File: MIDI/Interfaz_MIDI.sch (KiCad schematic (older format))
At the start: 22 parts, among them J1 DIN_5, J2 DIN_5, J3 DIN_5, U1 6N138, U2 4050

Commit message: Se continuan las correciones correspondientes a la 1ra revisión
> Se realizan los cambios necesarios para la utilización de la biblioteca de huellas autocontenidas.
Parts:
- C1, C2, C3: footprint Capacitors_SMD:C_0603_HandSoldering -> MIDI:C_0805_HandSoldering
- D1: footprint Diodes_THT:D_DO-35_SOD27_P7.62mm_Horizontal -> MIDI:D_DO-35_SOD27_P7.62mm_Horizontal
- FB1, FB2, FB3, FB4, FB5, FB6: footprint Resistors_SMD:R_0805_HandSoldering -> MIDI:FB_0805_HandSoldering
- R1, R4, R5, R7: footprint Resistors_SMD:R_0603_HandSoldering -> MIDI:R_0805_HandSoldering
- R2, R3, R6: footprint Resistors_SMD:R_0805_HandSoldering -> MIDI:R_0805_HandSoldering
- U1: footprint Housings_DIP:DIP-8_W7.62mm -> MIDI:DIP-8_W7.62mm_LongPads
- U2: footprint Housings_DIP:DIP-16_W7.62mm_LongPads -> MIDI:DIP-16_W7.62mm_LongPads
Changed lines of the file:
@@
 F 0 "FB3" H 3465 3185 60  0000 C CNN
 F 1 "1k @100MHz" H 3465 2935 60  0000 C CNN
-F 2 "Resistors_SMD:R_0805_HandSoldering" H 3465 3035 60  0001 C CNN
+F 2 "MIDI:FB_0805_HandSoldering" H 3465 3035 60  0001 C CNN
 F 3 "http://ds.yuden.co.jp/TYCOMPAS/ut/detail.do?productNo=BK2125HS102-T&fileName=BK2125HS102-T_SS&mode=specSheetDownload" H 3465 3035 60  0001 C CNN
 F 4 "FERRITE BEAD 1 KOHM 0805 1LN" H 0   0   50  0001 C CNN "Desc"
@@
 F 0 "FB1" H 3465 2375 60  0000 C CNN
 F 1 "1k @100MHz" H 3465 2125 60  0000 C CNN
-F 2 "Resistors_SMD:R_0805_HandSoldering" H 3465 2225 60  0001 C CNN
+F 2 "MIDI:FB_0805_HandSoldering" H 3465 2225 60  0001 C CNN
 F 3 "http://ds.yuden.co.jp/TYCOMPAS/ut/detail.do?productNo=BK2125HS102-T&fileName=BK2125HS102-T_SS&mode=specSheetDownload" H 3465 2225 60  0001 C CNN
 F 4 "FERRITE BEAD 1 KOHM 0805 1LN" H 0   0   50  0001 C CNN "Desc"
@@
 F 0 "FB2" H 8345 2850 60  0000 C CNN
 F 1 "1k @100MHz" H 8345 2600 60  0000 C CNN
-F 2 "Resistors_SMD:R_0805_HandSoldering" H 8345 2700 60  0001 C CNN
+F 2 "MIDI:FB_0805_HandSoldering" H 8345 2700 60  0001 C CNN
 F 3 "http://ds.yuden.co.jp/TYCOMPAS/ut/detail.do?productNo=BK2125HS102-T&fileName=BK2125HS102-T_SS&mode=specSheetDownload" H 8345 2700 60  0001 C CNN
 F 4 "FERRITE BEAD 1 KOHM 0805 1LN" H 0   0   50  0001 C CNN "Desc"
@@
 F 0 "FB4" H 8345 3650 60  0000 C CNN
 F 1 "1k @100MHz" H 8345 3400 60  0000 C CNN
-F 2 "Resistors_SMD:R_0805_HandSoldering" H 8345 3500 60  0001 C CNN
+F 2 "MIDI:FB_0805_HandSoldering" H 8345 3500 60  0001 C CNN
 F 3 "http://ds.yuden.co.jp/TYCOMPAS/ut/detail.do?productNo=BK2125HS102-T&fileName=BK2125HS102-T_SS&mode=specSheetDownload" H 8345 3500 60  0001 C CNN
 F 4 "FERRITE BEAD 1 KOHM 0805 1LN" H 0   0   50  0001 C CNN "Desc"
@@
 F 0 "R2" V 7815 2280 40  0000 C CNN
 F 1 "33R 0,5W" V 7742 2281 40  0000 C CNN
-F 2 "Resistors_SMD:R_0805_HandSoldering" V 7665 2280 30  0001 C CNN
+F 2 "MIDI:R_0805_HandSoldering" V 7665 2280 30  0001 C CNN
 F 3 "https://industrial.panasonic.com/cdbs/www-data/pdf/RDO0000/AOA0000C291.pdf" H 7735 2280 30  0001 C CNN
 F 4 "RES SMD 33 OHM 5% 1/2W 0805" H 0   0   50  0001 C CNN "Desc"
@@
 F 0 "R5" V 7575 3500 40  0000 C CNN
 F 1 "10R" V 7502 3501 40  0000 C CNN
-F 2 "Resistors_SMD:R_0603_HandSoldering" V 7425 3500 30  0001 C CNN
+F 2 "MIDI:R_0805_HandSoldering" V 7425 3500 30  0001 C CNN
 F 3 "http://www.rohm.com/web/global/datasheet/ESR01MZPF/esr-e" H 7495 3500 30  0001 C CNN
 F 4 "RES SMD 10 OHM 5% 1/4W 0603" H 0   0   50  0001 C CNN "Desc"
@@
 F 0 "FB6" H 8345 5875 60  0000 C CNN
 F 1 "1k @100MHz" H 8345 5625 60  0000 C CNN
-F 2 "Resistors_SMD:R_0805_HandSoldering" H 8345 5725 60  0001 C CNN
+F 2 "MIDI:FB_0805_HandSoldering" H 8345 5725 60  0001 C CNN
 F 3 "http://ds.yuden.co.jp/TYCOMPAS/ut/detail.do?productNo=BK2125HS102-T&fileName=BK2125HS102-T_SS&mode=specSheetDownload" H 8345 5725 60  0001 C CNN
 F 4 "FERRITE BEAD 1 KOHM 0805 1LN" H 0   0   50  0001 C CNN "Desc"
@@
 F 0 "R6" V 7815 4505 40  0000 C CNN
 F 1 "33R 0,5W" V 7742 4506 40  0000 C CNN
-F 2 "Resistors_SMD:R_0805_HandSoldering" V 7665 4505 30  0001 C CNN
+F 2 "MIDI:R_0805_HandSoldering" V 7665 4505 30  0001 C CNN
 F 3 "https://industrial.panasonic.com/cdbs/www-data/pdf/RDO0000/AOA0000C291.pdf" H 7735 4505 30  0001 C CNN
 F 4 "RES SMD 33 OHM 5% 1/2W 0805" H 0   0   50  0001 C CNN "Desc"
@@
 F 0 "R7" V 7575 5725 40  0000 C CNN
 F 1 "10R" V 7502 5726 40  0000 C CNN
-F 2 "Resistors_SMD:R_0603_HandSoldering" V 7425 5725 30  0001 C CNN
+F 2 "MIDI:R_0805_HandSoldering" V 7425 5725 30  0001 C CNN
 F 3 "http://www.rohm.com/web/global/datasheet/ESR01MZPF/esr-e" H 7495 5725 30  0001 C CNN
 F 4 "RES SMD 10 OHM 5% 1/4W 0603" H 0   0   50  0001 C CNN "Desc"
@@
 F 0 "FB5" H 8345 5075 60  0000 C CNN
 F 1 "1k @100MHz" H 8345 4825 60  0000 C CNN
-F 2 "Resistors_SMD:R_0805_HandSoldering" H 8345 4925 60  0001 C CNN
+F 2 "MIDI:FB_0805_HandSoldering" H 8345 4925 60  0001 C CNN
 F 3 "http://ds.yuden.co.jp/TYCOMPAS/ut/detail.do?productNo=BK2125HS102-T&fileName=BK2125HS102-T_SS&mode=specSheetDownload" H 8345 4925 60  0001 C CNN
 F 4 "FERRITE BEAD 1 KOHM 0805 1LN" H 0   0   50  0001 C CNN "Desc"
@@
 F 0 "U1" H 4655 2950 50  0000 L CNN
 F 1 "6N138" H 4730 2300 50  0000 L CNN
-F 2 "Housings_DIP:DIP-8_W7.62mm" H 4655 2250 50  0001 L CIN
+F 2 "MIDI:DIP-8_W7.62mm_LongPads" H 4655 2250 50  0001 L CIN
 F 3 "/Datasheets/6n138.pdf" V 4880 2600 50  0001 L CNN
 F 4 "OPTOISO 5KV DARL W/BASE 8DIP" H 0   0   50  0001 C CNN "Desc"
@@
 F 0 "D1" H 4065 2735 40  0000 C CNN
 F 1 "1N4148" H 4065 2535 40  0000 C CNN
-F 2 "Diodes_THT:D_DO-35_SOD27_P7.62mm_Horizontal" H 4065 2635 60  0001 C CNN
+F 2 "MIDI:D_DO-35_SOD27_P7.62mm_Horizontal" H 4065 2635 60  0001 C CNN
 F 3 "https://www.fairchildsemi.com/datasheets/1N/1N914.pdf" H 4065 2635 60  0001 C CNN
 F 4 "DIODE GEN PURP 100V 200MA DO35" H 0   0   50  0001 C CNN "Desc"
@@
 F 0 "C2" H 2310 3445 40  0000 L CNN
 F 1 "100nF" H 2316 3260 40  0000 L CNN
-F 2 "Capacitors_SMD:C_0603_HandSoldering" H 2348 3195 30  0001 C CNN
+F 2 "MIDI:C_0805_HandSoldering" H 2348 3195 30  0001 C CNN
 F 3 "http://search.murata.co.jp/Ceramy/image/img/A01X/G101/ENG/GRM188R71C104KA01-01.pdf" H 2310 3345 60  0001 C CNN
 F 4 "CAP CER 0.1UF 16V X7R 0603 " H 0   0   50  0001 C CNN "Desc"
@@
 F 0 "C1" H 1310 3445 40  0000 L CNN
 F 1 "100nF" H 1316 3260 40  0000 L CNN
-F 2 "Capacitors_SMD:C_0603_HandSoldering" H 1348 3195 30  0001 C CNN
+F 2 "MIDI:C_0805_HandSoldering" H 1348 3195 30  0001 C CNN
 F 3 "http://search.murata.co.jp/Ceramy/image/img/A01X/G101/ENG/GRM188R71C104KA01-01.pdf" H 1310 3345 60  0001 C CNN
 F 4 "CAP CER 0.1UF 16V X7R 0603 " H 0   0   50  0001 C CNN "Desc"
@@
 F 0 "R1" V 5675 2145 40  0000 C CNN
 F 1 "1K" V 5602 2146 40  0000 C CNN
-F 2 "Resistors_SMD:R_0603_HandSoldering" V 5525 2145 30  0001 C CNN
+F 2 "MIDI:R_0805_HandSoldering" V 5525 2145 30  0001 C CNN
 F 3 "http://www.rohm.com/web/global/datasheet/ESR01MZPF/esr-e" H 5595 2145 30  0001 C CNN
 F 4 "RES SMD 1K OHM 5% 1/4W 0603 " H 0   0   50  0001 C CNN "Desc"
@@
 F 0 "R4" V 5465 3285 40  0000 C CNN
 F 1 "4K7" V 5392 3286 40  0000 C CNN
-F 2 "Resistors_SMD:R_0603_HandSoldering" V 5315 3285 30  0001 C CNN
+F 2 "MIDI:R_0805_HandSoldering" V 5315 3285 30  0001 C CNN
 F 3 "http://www.rohm.com/web/global/datasheet/ESR01MZPF/esr-e" H 5385 3285 30  0001 C CNN
 F 4 "RES SMD 4.7K OHM 5% 1/4W 0603 " H 0   0   50  0001 C CNN "Desc"
@@
 F 0 "U2" H 2045 5165 50  0000 C CNN
 F 1 "4050" H 2040 4925 50  0000 C CNN
-F 2 "Housings_DIP:DIP-16_W7.62mm_LongPads" H 1850 5050 60  0001 C CNN
+F 2 "MIDI:DIP-16_W7.62mm_LongPads" H 1850 5050 60  0001 C CNN
 F 3 "/Datasheets/cd4050b.pdf" H 1850 5050 60  0001 C CNN
 F 4 "IC BUFF/CONVERTER HEX 16DIP" H -4695 1550 50  0001 C CNN "Desc"
@@
 F 0 "U2" H 6740 2815 50  0000 C CNN
 F 1 "4050" H 6735 2575 50  0000 C CNN
-F 2 "Housings_DIP:DIP-16_W7.62mm_LongPads" H 6545 2700 60  0001 C CNN
+F 2 "MIDI:DIP-16_W7.62mm_LongPads" H 6545 2700 60  0001 C CNN
 F 3 "/Datasheets/cd4050b.pdf" H 6545 2700 60  0001 C CNN
 F 4 "IC BUFF/CONVERTER HEX 16DIP" H 0   0   50  0001 C CNN "Desc"
@@
 F 0 "U2" H 6740 3615 50  0000 C CNN
 F 1 "4050" H 6735 3375 50  0000 C CNN
-F 2 "Housings_DIP:DIP-16_W7.62mm_LongPads" H 6545 3500 60  0001 C CNN
+F 2 "MIDI:DIP-16_W7.62mm_LongPads" H 6545 3500 60  0001 C CNN
 F 3 "/Datasheets/cd4050b.pdf" H 6545 3500 60  0001 C CNN
 F 4 "IC BUFF/CONVERTER HEX 16DIP" H 0   -2225 50  0001 C CNN "Desc"
@@
 F 0 "R3" V 2865 3035 40  0000 C CNN
 F 1 "220R" V 2792 3036 40  0000 C CNN
-F 2 "Resistors_SMD:R_0805_HandSoldering" V 2715 3035 30  0001 C CNN
+F 2 "MIDI:R_0805_HandSoldering" V 2715 3035 30  0001 C CNN
 F 3 "http://www.rohm.com/web/global/datasheet/ESR01MZPF/esr-e" H 2785 3035 30  0001 C CNN
 F 4 "RES SMD 220 OHM 5% 1/4W 0603" H 0   0   50  0001 C CNN "Desc"
@@
 F 0 "C3" H 3660 5030 40  0000 L CNN
 F 1 "100nF" H 3666 4845 40  0000 L CNN
-F 2 "Capacitors_SMD:C_0603_HandSoldering" H 3698 4780 30  0001 C CNN
+F 2 "MIDI:C_0805_HandSoldering" H 3698 4780 30  0001 C CNN
 F 3 "http://search.murata.co.jp/Ceramy/image/img/A01X/G101/ENG/GRM188R71C104KA01-01.pdf" H 3660 4930 60  0001 C CNN
 F 4 "CAP CER 0.1UF 16V X7R 0603 " H -2900 -2150 50  0001 C CNN "Desc"
@@
 F 0 "U2" H 2045 4765 50  0000 C CNN
 F 1 "4050" H 2040 4525 50  0000 C CNN
-F 2 "Housings_DIP:DIP-16_W7.62mm_LongPads" H 1850 4650 60  0001 C CNN
+F 2 "MIDI:DIP-16_W7.62mm_LongPads" H 1850 4650 60  0001 C CNN
 F 3 "/Datasheets/cd4050b.pdf" H 1850 4650 60  0001 C CNN
 F 4 "IC BUFF/CONVERTER HEX 16DIP" H 0   0   50  0001 C CNN "Desc"
@@
 F 0 "U2" H 6740 5840 50  0000 C CNN
 F 1 "4050" H 6735 5600 50  0000 C CNN
-F 2 "Housings_DIP:DIP-16_W7.62mm_LongPads" H 6545 5725 60  0001 C CNN
+F 2 "MIDI:DIP-16_W7.62mm_LongPads" H 6545 5725 60  0001 C CNN
 F 3 "/Datasheets/cd4050b.pdf" H 6545 5725 60  0001 C CNN
 F 4 "IC BUFF/CONVERTER HEX 16DIP" H 4695 675 50  0001 C CNN "Desc"
@@
 F 0 "U2" H 2045 5565 50  0000 C CNN
 F 1 "4050" H 2040 5325 50  0000 C CNN
-F 2 "Housings_DIP:DIP-16_W7.62mm_LongPads" H 1850 5450 60  0001 C CNN
+F 2 "MIDI:DIP-16_W7.62mm_LongPads" H 1850 5450 60  0001 C CNN
 F 3 "/Datasheets/cd4050b.pdf" H 1850 5450 60  0001 C CNN
 F 4 "IC BUFF/CONVERTER HEX 16DIP" H 0   0   50  0001 C CNN "Desc"

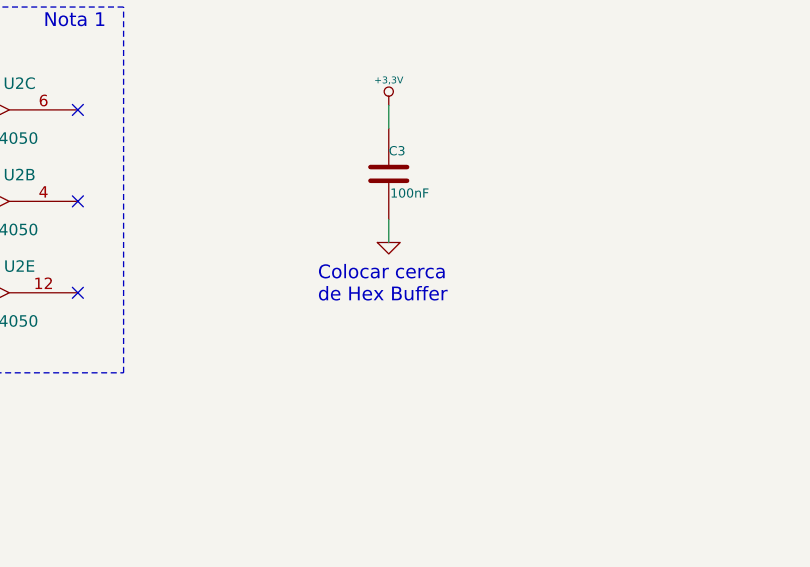
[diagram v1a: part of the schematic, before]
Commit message: Se avanza con primera iteración de ruteo
> Se terminan de rutear conexiones para estudiar factibilidad de placement.
> Para facilitar el ruteo se realizan los siguientes cambios:
  > Se desconecta pin redundante de tact-switch's para permitir la conexión entre planos de masa.
  > Se desconectan pines del conector derecho de forma que no requieran ser ruteados a los homologos del conector izquierdo.
  > Se intercambian unidades F y D del componente 40106.
  > Se agrupan señales de los interruptores de los encoders en vez de intercalarlos con las señales de encoder, propiamente dicho, de cada uno. Se rutean a pines superiores en el conector izquierdo, mientras se desplazan las restantes señales hacia abajo.

> Se aguarda comentarios de los revisores para emprolijar, embellecer y mejorar el ruteo.
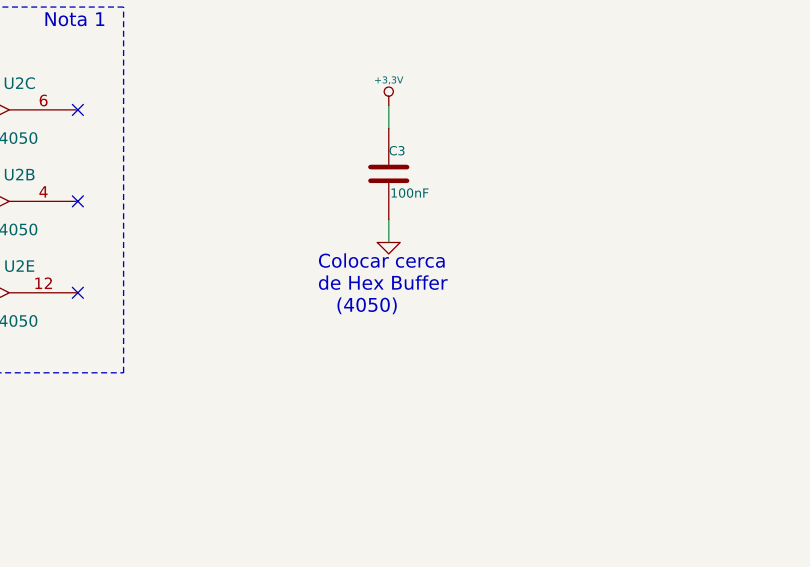
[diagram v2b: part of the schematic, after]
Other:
- note added: "Colocar cerca\nde Hex Buffer\n (4050)"
- note removed: "Colocar cerca\nde Hex Buffer"
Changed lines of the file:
@@
 Text Notes 9620 2230 0    60   ~ 0
 MIDI THRU
-Text Notes 3350 5500 0    60   ~ 0
-Colocar cerca\nde Hex Buffer
+Text Notes 3350 5550 0    60   ~ 0
+Colocar cerca\nde Hex Buffer\n   (4050)
 Text Notes 2150 4300 0    60   ~ 0
 Nota 1

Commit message: Se modifican campos de componentes
> Se realizan los cambios en los campos de kiCost para reflejar los cambios de footprints (de 0603 a 0805).
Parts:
- C1, C2, C3: Desc CAP CER 0.1UF 16V X7R 0603 -> CAP CER 0.1UF 50V X7R 0805; Digikey# 490-1532-1-ND -> 311-1140-1-ND; Manf Murata Electronics North America -> Yageo; Manf# GRM188R71C104KA01D -> CC0805KRX7R9BB104; Mouser# 81-GRM39X104K16 -> 603-CC805KRX7R9BB104
- R1: Desc RES SMD 1K OHM 5% 1/4W 0603 -> RES SMD 1K OHM 1% 1/2W 0805; Digikey# RHM1.0KDCT-ND -> P16885CT-ND; Manf Rohm Semiconductor -> Panasonic Electronic Components; Manf# ESR03EZPJ102 -> ERJ-P6WF1001V; Mouser# 755-ESR03EZPJ102 -> 667-ERJ-P6WF1001V
- R3: Desc RES SMD 220 OHM 5% 1/4W 0603 -> RES SMD 220 OHM 5% 1/2W 0805; Digikey# RHM220DCT-ND -> P220ADCT-ND; Manf Rohm Semiconductor -> Panasonic Electronic Components; Manf# ESR03EZPJ221 -> ERJ-P06J221V; Mouser# 755-ESR03EZPJ221 -> 667-ERJ-P06J221V
- R4: Desc RES SMD 4.7K OHM 5% 1/4W 0603 -> RES SMD 4.7K OHM 5% 1/2W 0805; Digikey# RHM4.7KDCT-ND -> P4.7KADCT-ND; Manf Rohm Semiconductor -> Panasonic Electronic Components; Manf# ESR03EZPJ472 -> ERJ-P06J472V; Mouser# 755-ESR03EZPJ472 -> 667-ERJ-P06J472V
- R5, R7: Desc RES SMD 10 OHM 5% 1/4W 0603 -> RES SMD 1K OHM 1% 1/4W 0805; Digikey# RHM10DCT-ND -> CRS0805-FX-1001ELFCT-ND; Manf Rohm Semiconductor -> Bourns Inc.; Manf# ESR03EZPJ100 -> CRS0805-FX-1001ELF; Mouser# 755-ESR03EZPJ100 -> 652-CRS0805FX1001ELF

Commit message: Correcciones menores en campos para BOM
> Se corrigen error observados luego de la generación de la BOM.
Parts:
- C1, C2, C3: Description (none) -> CAP CER 0.1UF 50V X7R 0805
- D1: Description (none) -> DIODE GEN PURP 100V 200MA DO35; Manf# 1N4148 -> 1N4148
- FB1, FB2, FB3, FB4, FB5, FB6: Description (none) -> FERRITE BEAD 1 KOHM 0805 1LN
- J1, J2, J3: Desc CONN DIN 5POS FEMALE SHIELDED -> CONN DIN 5POS FEMALE SHIELDED; Description (none) -> CONN DIN 5POS FEMALE SHIELDED; Digikey# CP-7050-ND -> CP-7050-ND
- R1: Description (none) -> RES SMD 1K OHM 1% 1/2W 0805
- R2, R6: Description (none) -> RES SMD 33 OHM 5% 1/2W 0805
- R3: Description (none) -> RES SMD 220 OHM 5% 1/2W 0805
- R4: Description (none) -> RES SMD 4.7K OHM 5% 1/2W 0805
- R5, R7: Description (none) -> RES SMD 1K OHM 1% 1/4W 0805
- U1: Description (none) -> OPTOISO 5KV DARL W/BASE 8DIP
- U2: Description (none) -> IC BUFF/CONVERTER HEX 16DIP

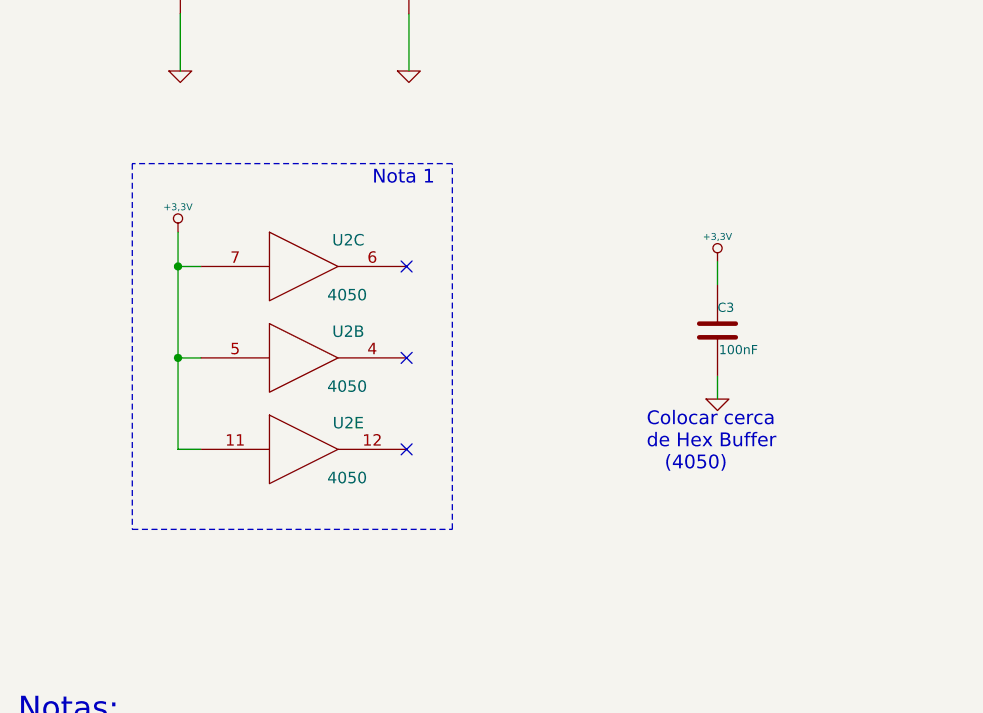
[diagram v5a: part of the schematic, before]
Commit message: Se finalizan los cambios según las revisiones
> Se realizan cambios segun detalles en archivos de revisiones.
> Se abandona requisito para asegurar fabricación artesanal por lo que se comienzan a utilizar los orificios metalizados para rutear.
> Se cambia la tensión de fijación de las compuertas no utilizadas en el 4050 para mejorar el plano de masa debajo del mismo.
> Se genera la versión 1.0 del diseño.
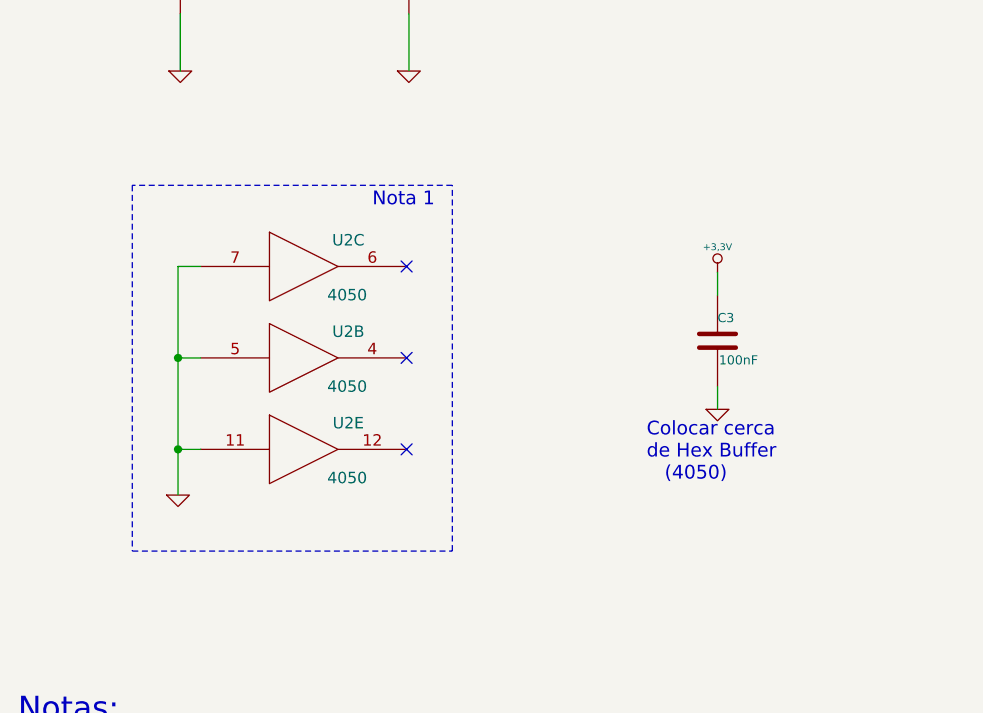
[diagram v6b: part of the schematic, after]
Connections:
- net +3.3V: no longer U2.11, U2.5, U2.7
- net GND: now also U2.11, U2.5, U2.7
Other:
- moved on the sheet: C3
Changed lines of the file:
@@
 L GND #PWR014
 U 1 1 592CE7E7
-P 3660 5230
-F 0 "#PWR014" H 3660 5230 30  0001 C CNN
-F 1 "GND" H 3660 5160 30  0001 C CNN
-F 2 "" H 3660 5230 60  0000 C CNN
-F 3 "" H 3660 5230 60  0000 C CNN
-	1    3660 5230
+P 3660 5275
+F 0 "#PWR014" H 3660 5275 30  0001 C CNN
+F 1 "GND" H 3660 5205 30  0001 C CNN
+F 2 "" H 3660 5275 60  0000 C CNN
+F 3 "" H 3660 5275 60  0000 C CNN
+	1    3660 5275
 	1    0    0    -1
 $EndComp
@@
 L +3,3V #PWR015
 U 1 1 592CE837
-P 3660 4630
-F 0 "#PWR015" H 3660 4590 30  0001 C CNN
-F 1 "+3,3V" H 3660 4740 30  0000 C CNN
-F 2 "" H 3660 4630 60  0000 C CNN
-F 3 "" H 3660 4630 60  0000 C CNN
-	1    3660 4630
+P 3660 4675
+F 0 "#PWR015" H 3660 4635 30  0001 C CNN
+F 1 "+3,3V" H 3660 4785 30  0000 C CNN
+F 2 "" H 3660 4675 60  0000 C CNN
+F 3 "" H 3660 4675 60  0000 C CNN
+	1    3660 4675
 	1    0    0    -1
 $EndComp
@@
 L C C3
 U 1 1 592CE8FA
-P 3660 4930
-F 0 "C3" H 3660 5030 40  0000 L CNN
-F 1 "100nF" H 3666 4845 40  0000 L CNN
-F 2 "MIDI:C_0805_HandSoldering" H 3698 4780 30  0001 C CNN
-F 3 "http://www.yageo.com/documents/recent/UPY-GPHC_X7R_6.3V-to-50V_18.pdf" H 3660 4930 60  0001 C CNN
-F 4 "CAP CER 0.1UF 50V X7R 0805" H 0   0   50  0001 C CNN "Desc"
-F 5 "CAP CER 0.1UF 50V X7R 0805" H 0   0   50  0001 C CNN "Description"
-F 6 "311-1140-1-ND" H -2900 -2150 50  0001 C CNN "Digikey#"
-F 7 "Yageo" H -2900 -2150 50  0001 C CNN "Manf"
-F 8 "CC0805KRX7R9BB104" H -2900 -2150 50  0001 C CNN "Manf#"
-F 9 "603-CC805KRX7R9BB104" H -2900 -2150 50  0001 C CNN "Mouser#"
-	1    3660 4930
-	1    0    0    -1
-$EndComp
-$Comp
-L +3,3V #PWR016
-U 1 1 592EB13E
-P 1300 4500
-F 0 "#PWR016" H 1300 4460 30  0001 C CNN
-F 1 "+3,3V" H 1300 4610 30  0000 C CNN
-F 2 "" H 1300 4500 60  0000 C CNN
-F 3 "" H 1300 4500 60  0000 C CNN
-	1    1300 4500
+P 3660 4975
+F 0 "C3" H 3660 5075 40  0000 L CNN
+F 1 "100nF" H 3666 4890 40  0000 L CNN
+F 2 "MIDI:C_0805_HandSoldering" H 3698 4825 30  0001 C CNN
+F 3 "http://www.yageo.com/documents/recent/UPY-GPHC_X7R_6.3V-to-50V_18.pdf" H 3660 4975 60  0001 C CNN
+F 4 "CAP CER 0.1UF 50V X7R 0805" H 0   45  50  0001 C CNN "Desc"
+F 5 "CAP CER 0.1UF 50V X7R 0805" H 0   45  50  0001 C CNN "Description"
+F 6 "311-1140-1-ND" H -2900 -2105 50  0001 C CNN "Digikey#"
+F 7 "Yageo" H -2900 -2105 50  0001 C CNN "Manf"
+F 8 "CC0805KRX7R9BB104" H -2900 -2105 50  0001 C CNN "Manf#"
+F 9 "603-CC805KRX7R9BB104" H -2900 -2105 50  0001 C CNN "Mouser#"
+	1    3660 4975
 	1    0    0    -1
 $EndComp
@@
 Text Notes 9620 2230 0    60   ~ 0
 MIDI THRU
-Text Notes 3350 5550 0    60   ~ 0
+Text Notes 3350 5595 0    60   ~ 0
 Colocar cerca\nde Hex Buffer\n   (4050)
-Text Notes 2150 4300 0    60   ~ 0
+Text Notes 2150 4395 0    60   ~ 0
 Nota 1
 Text Notes 600  6650 0    100  ~ 0
@@
 	6495 5825 6495 5925
 Wire Wire Line
-	3660 5130 3660 5230
-Wire Wire Line
-	3660 4730 3660 4630
-Wire Wire Line
-	1300 4500 1300 5450
+	3660 5175 3660 5275
+Wire Wire Line
+	3660 4775 3660 4675
 Wire Wire Line
 	1300 5450 1400 5450
@@
 	1400 5050 1300 5050
 Wire Notes Line
-	1100 4200 1100 5800
-Wire Notes Line
-	1100 5800 2500 5800
-Wire Notes Line
-	2500 5800 2500 4200
-Wire Notes Line
-	2500 4200 1100 4200
+	1100 4295 1100 5895
+Wire Notes Line
+	1100 5895 2500 5895
+Wire Notes Line
+	2500 5895 2500 4295
+Wire Notes Line
+	2500 4295 1100 4295
 Connection ~ 4065 3035
 Connection ~ 4065 2225
 Connection ~ 5595 2700
 Connection ~ 5845 2700
-Connection ~ 1300 4650
 Connection ~ 1300 5050
 NoConn ~ 1910 2025
@@
 NoConn ~ 2300 5050
 NoConn ~ 2300 5450
+$Comp
+L GND #PWR?
+U 1 1 5998B214
+P 1300 5650
+F 0 "#PWR?" H 1300 5650 30  0001 C CNN
+F 1 "GND" H 1300 5580 30  0001 C CNN
+F 2 "" H 1300 5650 60  0000 C CNN
+F 3 "" H 1300 5650 60  0000 C CNN
+	1    1300 5650
+	1    0    0    -1
+$EndComp
+Connection ~ 1300 5450
+Wire Wire Line
+	1300 4650 1300 5650
 $EndSCHEMATC
